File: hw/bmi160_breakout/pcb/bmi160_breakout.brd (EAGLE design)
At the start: 10 x 12 mm, 4 parts, among them CON1 B4B-ZR, U1 BMI160LGA14

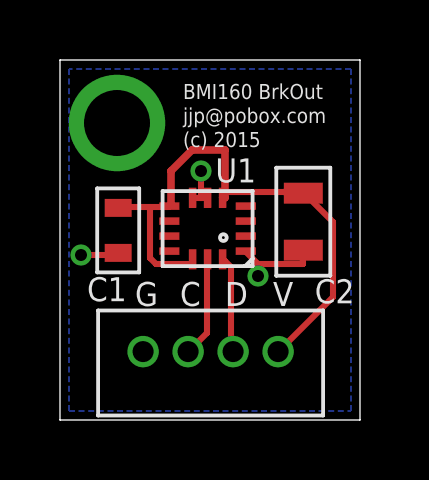
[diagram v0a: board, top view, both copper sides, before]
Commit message: BMI160 breakout: Add a solder jumper to select I2C address.  Add silk to denote orientation.
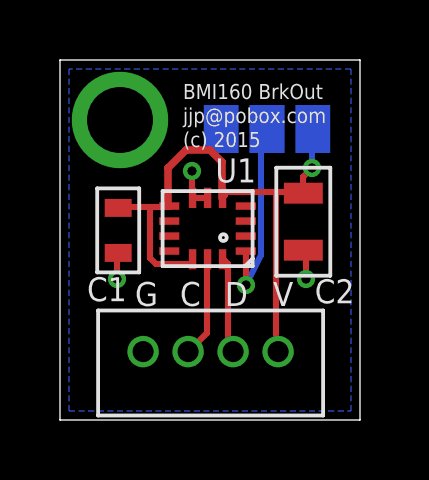
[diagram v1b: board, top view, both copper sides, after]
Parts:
- added SJ1: (no value), jumper:SJ_2
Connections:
- new net N$1: SJ1.2, U1.1
- net GND: now also SJ1.3; no longer U1.1
- net VDD: now also SJ1.1
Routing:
- net N$1: track 0.00 -> 6.65 mm, vias 0 -> 1
- net GND: track 5.64 -> 3.29 mm
- net VDD: track 19.3 -> 20.3 mm, vias 0 -> 1
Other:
- board text added: "0"
- board text added: "1"
- board text added: "SA0"
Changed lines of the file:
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@@
 <text x="4" y="3.8" size="0.8" layer="21">C</text>
 <text x="5.5" y="3.8" size="0.8" layer="21">D</text>
-<wire x1="7" y1="9.75" x2="7" y2="9" width="0.1" layer="22"/>
-<wire x1="7" y1="9" x2="7.3" y2="9.3" width="0.1" layer="22"/>
-<wire x1="7" y1="9" x2="6.7" y2="9.3" width="0.1" layer="22"/>
-<wire x1="8" y1="10" x2="7.7" y2="10.3" width="0.1" layer="22"/>
-<wire x1="8" y1="10" x2="7.7" y2="9.7" width="0.1" layer="22"/>
-<text x="6.7" y="8.5" size="0.8" layer="22" rot="MR0">x</text>
-<text x="8.7" y="10.2" size="0.8" layer="22" rot="MR0">y</text>
-<circle x="7" y="10" radius="0.22360625" width="0.1" layer="22"/>
-<wire x1="8" y1="10" x2="7.25" y2="10" width="0.1" layer="22"/>
-<wire x1="6.8" y1="10.2" x2="7.2" y2="9.8" width="0.1" layer="22"/>
-<wire x1="6.8" y1="9.8" x2="7.2" y2="10.2" width="0.1" layer="22"/>
-<text x="6.7" y="10.3" size="0.8" layer="22" rot="MR0">z</text>
+<wire x1="7" y1="6.75" x2="7" y2="6" width="0.1" layer="22"/>
+<wire x1="7" y1="6" x2="7.3" y2="6.3" width="0.1" layer="22"/>
+<wire x1="7" y1="6" x2="6.7" y2="6.3" width="0.1" layer="22"/>
+<wire x1="8" y1="7" x2="7.7" y2="7.3" width="0.1" layer="22"/>
+<wire x1="8" y1="7" x2="7.7" y2="6.7" width="0.1" layer="22"/>
+<text x="6.7" y="5.5" size="0.8" layer="22" rot="MR0">x</text>
+<text x="8.7" y="7.2" size="0.8" layer="22" rot="MR0">y</text>
+<circle x="7" y="7" radius="0.22360625" width="0.1" layer="22"/>
+<wire x1="8" y1="7" x2="7.25" y2="7" width="0.1" layer="22"/>
+<wire x1="6.8" y1="7.2" x2="7.2" y2="6.8" width="0.1" layer="22"/>
+<wire x1="6.8" y1="6.8" x2="7.2" y2="7.2" width="0.1" layer="22"/>
+<text x="6.7" y="7.3" size="0.8" layer="22" rot="MR0">z</text>
+<text x="7.9" y="10.9" size="0.8" layer="22" font="vector" rot="MR0">SA0</text>
+<text x="9.1" y="10.9" size="0.8" layer="22" font="vector" rot="MR0">1</text>
+<text x="5.3" y="10.9" size="0.8" layer="22" font="vector" rot="MR0">0</text>
 </plain>
 <attributes>
@@
 <element name="U1" library="bmi160_breakout" package="LGA14" value="BMI160LGA14" x="4.92" y="6.38" smashed="yes" rot="R180">
 <attribute name="NAME" x="5.18" y="7.92" size="0.8" layer="21" ratio="10"/>
+<attribute name="MOUSER_PN" value="262-BMI160" x="4.92" y="6.38" size="1.778" layer="27" rot="R180" display="off"/>
+<attribute name="MPN" value="BMI160" x="4.92" y="6.38" size="1.778" layer="27" rot="R180" display="off"/>
 </element>
 <element name="C1" library="mfpassives" package="C0603" value=".1uF" x="1.94" y="6.32" smashed="yes" rot="R270">
@@
 </element>
 <element name="CON1" library="bmi160_breakout" package="B4B-ZR" value="B4B-ZR" x="1.27" y="3.58" smashed="yes"/>
+<element name="SJ1" library="jumper" package="SJ_2" value="" x="6.9" y="9.7" smashed="yes" rot="MR0">
+<attribute name="VALUE" x="7.0001" y="9.7" size="0.02" layer="28" rot="MR0"/>
+</element>
 </elements>
 <signals>
@@
 <contactref element="C1" pad="P$2"/>
 <contactref element="C2" pad="P$2"/>
-<contactref element="U1" pad="1"/>
 <contactref element="CON1" pad="4"/>
 <polygon width="0.254" layer="16">
@@
 <vertex x="9.7" y="11.7"/>
 </polygon>
-<via x="6.6" y="4.8" extent="1-16" drill="0.4"/>
-<via x="4.7" y="8.3" extent="1-16" drill="0.4"/>
-<via x="0.7" y="5.5" extent="1-16" drill="0.4"/>
-<wire x1="4.9" y1="7.4" x2="4.7" y2="7.4" width="0.2032" layer="1"/>
-<wire x1="4.7" y1="7.4" x2="4.5" y2="7.4" width="0.2032" layer="1"/>
+<contactref element="SJ1" pad="3"/>
+<via x="1.9" y="4.7" extent="1-16" drill="0.3048"/>
+<via x="4.4" y="8.3" extent="1-16" drill="0.3048"/>
+<via x="8.2" y="4.7" extent="1-16" drill="0.3048"/>
+<wire x1="4.9" y1="7.4" x2="4.5" y2="7.4" width="0.2032" layer="1"/>
 <wire x1="4.5" y1="7.4" x2="4.42" y2="7.405" width="0.2032" layer="1"/>
 <wire x1="4.9" y1="7.4" x2="4.92" y2="7.405" width="0.2032" layer="1"/>
-<wire x1="6.6" y1="5.2" x2="6.2" y2="5.6" width="0.2032" layer="1"/>
-<wire x1="6.6" y1="4.8" x2="6.6" y2="5.2" width="0.2032" layer="1"/>
-<wire x1="6.2" y1="5.6" x2="6.195" y2="5.63" width="0.2032" layer="1"/>
-<wire x1="8.1" y1="5.2" x2="6.6" y2="5.2" width="0.2032" layer="1"/>
-<wire x1="8.1" y1="5.6" x2="8.1" y2="5.2" width="0.2032" layer="1"/>
-<wire x1="8.1" y1="5.6" x2="8.11" y2="5.66" width="0.2032" layer="1"/>
-<wire x1="4.7" y1="8.3" x2="4.7" y2="7.4" width="0.2032" layer="1"/>
-<wire x1="0.7" y1="5.5" x2="1.9" y2="5.5" width="0.2032" layer="1"/>
+<wire x1="4.4" y1="8.3" x2="4.4" y2="7.5" width="0.2032" layer="1"/>
+<wire x1="4.4" y1="7.5" x2="4.42" y2="7.405" width="0.2032" layer="1"/>
+<wire x1="1.9" y1="4.7" x2="1.9" y2="5.5" width="0.2032" layer="1"/>
 <wire x1="1.9" y1="5.5" x2="1.94" y2="5.57" width="0.2032" layer="1"/>
+<wire x1="8.2" y1="4.7" x2="8.2" y2="5.6" width="0.2032" layer="1"/>
+<wire x1="8.2" y1="5.6" x2="8.11" y2="5.66" width="0.2032" layer="1"/>
 </signal>
 <signal name="VDD">
@@
 <contactref element="U1" pad="12"/>
 <contactref element="CON1" pad="1"/>
+<contactref element="SJ1" pad="1"/>
 <wire x1="2" y1="7.1" x2="3" y2="7.1" width="0.2032" layer="1"/>
 <wire x1="3" y1="7.1" x2="3.6" y2="7.1" width="0.2032" layer="1"/>
 <wire x1="3.6" y1="7.1" x2="3.645" y2="7.13" width="0.2032" layer="1"/>
 <wire x1="2" y1="7.1" x2="1.94" y2="7.07" width="0.2032" layer="1"/>
-<wire x1="5.5" y1="7.6" x2="8.1" y2="7.6" width="0.2032" layer="1"/>
+<wire x1="5.4" y1="7.4" x2="5.42" y2="7.405" width="0.2032" layer="1"/>
+<wire x1="5.5" y1="7.6" x2="7.2" y2="7.6" width="0.2032" layer="1"/>
+<wire x1="7.2" y1="7.6" x2="8.1" y2="7.6" width="0.2032" layer="1"/>
 <wire x1="5.5" y1="7.5" x2="5.5" y2="7.6" width="0.2032" layer="1"/>
 <wire x1="8.1" y1="7.6" x2="8.11" y2="7.56" width="0.2032" layer="1"/>
@@
 <wire x1="4.4" y1="5.3" x2="4.4" y2="5.2" width="0.2032" layer="1"/>
 <wire x1="4.4" y1="5.3" x2="4.42" y2="5.355" width="0.2032" layer="1"/>
-<wire x1="9.1" y1="4.1" x2="7.3" y2="2.3" width="0.2032" layer="1"/>
-<wire x1="9.1" y1="6.6" x2="9.1" y2="4.1" width="0.2032" layer="1"/>
-<wire x1="8.2" y1="7.5" x2="9.1" y2="6.6" width="0.2032" layer="1"/>
-<wire x1="7.3" y1="2.3" x2="7.27" y2="2.28" width="0.2032" layer="1"/>
-<wire x1="8.2" y1="7.5" x2="8.11" y2="7.56" width="0.2032" layer="1"/>
-<wire x1="5.42" y1="7.405" x2="5.5" y2="7.405" width="0.254" layer="1"/>
-<wire x1="5.5" y1="7.405" x2="5.5" y2="9" width="0.254" layer="1"/>
-<wire x1="5.5" y1="9" x2="4.4" y2="9" width="0.254" layer="1"/>
-<wire x1="4.4" y1="9" x2="3.7" y2="8.3" width="0.254" layer="1"/>
-<wire x1="3.7" y1="8.3" x2="3.7" y2="7.185" width="0.254" layer="1"/>
-<wire x1="3.7" y1="7.185" x2="3.645" y2="7.13" width="0.254" layer="1"/>
+<wire x1="8.4" y1="8.4" x2="8.4" y2="9.7" width="0.2032" layer="16"/>
+<wire x1="8.1" y1="8.1" x2="8.4" y2="8.4" width="0.2032" layer="1"/>
+<wire x1="8.1" y1="7.7" x2="8.1" y2="8.1" width="0.2032" layer="1"/>
+<wire x1="8.4" y1="9.7" x2="8.424" y2="9.7" width="0.2032" layer="16"/>
+<wire x1="8.1" y1="7.7" x2="8.11" y2="7.56" width="0.2032" layer="1"/>
+<wire x1="7.2" y1="7.6" x2="7.2" y2="2.3" width="0.2032" layer="1"/>
+<wire x1="7.2" y1="2.3" x2="7.27" y2="2.28" width="0.2032" layer="1"/>
+<via x="8.4" y="8.4" extent="1-16" drill="0.3048"/>
+<wire x1="5.4" y1="7.4" x2="5.4" y2="8.6" width="0.254" layer="1"/>
+<wire x1="5.4" y1="8.6" x2="5" y2="9" width="0.254" layer="1"/>
+<wire x1="5" y1="9" x2="4.2" y2="9" width="0.254" layer="1"/>
+<wire x1="4.2" y1="9" x2="3.6" y2="8.4" width="0.254" layer="1"/>
+<wire x1="3.6" y1="8.4" x2="3.6" y2="7.175" width="0.254" layer="1"/>
+<wire x1="3.6" y1="7.175" x2="3.645" y2="7.13" width="0.254" layer="1"/>
 </signal>
 <signal name="SDA">
 <contactref element="U1" pad="14"/>
 <contactref element="CON1" pad="2"/>
-<wire x1="5.7" y1="5.1" x2="5.5" y2="5.3" width="0.2032" layer="1"/>
-<wire x1="5.7" y1="2.3" x2="5.7" y2="5.1" width="0.2032" layer="1"/>
+<wire x1="5.6" y1="5.2" x2="5.5" y2="5.3" width="0.2032" layer="1"/>
+<wire x1="5.6" y1="2.4" x2="5.6" y2="5.2" width="0.2032" layer="1"/>
+<wire x1="5.7" y1="2.3" x2="5.6" y2="2.4" width="0.2032" layer="1"/>
 <wire x1="5.5" y1="5.3" x2="5.42" y2="5.355" width="0.2032" layer="1"/>
 <wire x1="5.7" y1="2.3" x2="5.77" y2="2.28" width="0.2032" layer="1"/>
@@
 </signal>
 <signal name="N$3">
-<via x="1.9" y="9.9" extent="1-16" drill="2.2"/>
+<via x="2" y="10" extent="1-16" drill="2.2"/>
+</signal>
+<signal name="N$1">
+<contactref element="U1" pad="1"/>
+<contactref element="SJ1" pad="2"/>
+<wire x1="6.2" y1="4.5" x2="6.2" y2="5.6" width="0.2032" layer="1"/>
+<wire x1="6.7" y1="5.5" x2="6.2" y2="4.5" width="0.2032" layer="16"/>
+<wire x1="6.7" y1="9.7" x2="6.7" y2="5.5" width="0.2032" layer="16"/>
+<wire x1="6.9" y1="9.7" x2="6.7" y2="9.7" width="0.2032" layer="16"/>
+<wire x1="6.2" y1="5.6" x2="6.195" y2="5.63" width="0.2032" layer="1"/>
+<via x="6.2" y="4.5" extent="1-16" drill="0.3048"/>
 </signal>
 </signals>
